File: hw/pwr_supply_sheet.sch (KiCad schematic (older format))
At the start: 12 parts

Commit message: porting uv0a_hds pcb to uw_display
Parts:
- removed C11: 10nF, kemet:Kemet-CAPC1608X85N, symbol 10nF
- removed C13, C9: 100nF, kemet:Kemet-CAPC1608X85N, symbol 100nF
- removed L201: IND_744045210, usevolt:IND_744045210, symbol IND_744045210
- removed VR1: LM2671SOIC8, usevolt:SOIC8, symbol LM2671SOIC8-RESCUE-display
- added C203, C204, C205: 100nF, kemet:0603, symbol 100nF
- added L201: INDUCTOR_SDR1005-101KL, usevolt:INDUCTOR_BOURNS_10X13X5MM, symbol INDUCTOR_SDR1005-101KL
- added VR201: LM2671SOIC8, usevolt:SOIC8, symbol LM2671SOIC8
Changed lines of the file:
@@
 $Descr A4 11693 8268
 encoding utf-8
-Sheet 2 3
+Sheet 2 5
 Title "Power supply"
 Date "2016-08-20"
@@
 	1    3000 4050
 	0    -1   -1   0
-$EndComp
-$Comp
-L 100nF C9
-U 1 1 57B8217A
-P 3200 3950
-F 0 "C9" V 3208 4023 45  0000 L CNN
-F 1 "100nF" V 3292 4023 45  0000 L CNN
-F 2 "kemet:Kemet-CAPC1608X85N" H 3230 4100 20  0001 C CNN
-F 3 "http://www.farnell.com/datasheets/2062872.pdf?_ga=1.250530118.1948984246.1460023966" H 3104 3959 60  0001 C CNN
-F 4 "1288255" H 3504 4359 60  0001 C CNN "1st Source Part Number"
-F 5 "C0603C104K5RACTU" H 3304 4159 60  0001 C CNN "Manufacturer Part Number"
-F 6 "Farnell" H 3404 4259 60  0001 C CNN "1st Source"
-F 7 "KEMET" H 3204 4059 60  0001 C CNN "Manufacturer"
-	1    3200 3950
-	0    1    1    0
-$EndComp
-$Comp
-L LM2671SOIC8-RESCUE-display VR1
-U 1 1 57B82261
-P 4850 4150
-AR Path="/57B82261" Ref="VR1"  Part="1"
-AR Path="/57B81D4F/57B82261" Ref="VR1"  Part="1"
-F 0 "VR1" H 5050 4804 45  0000 C CNN
-F 1 "LM2671SOIC8" H 5050 4720 45  0000 C CNN
-F 2 "usevolt:SOIC8" H 4880 4300 20  0001 C CNN
-F 3 "http://www.farnell.com/datasheets/1902681.pdf?_ga=1.246738500.1948984246.1460023966" H 4650 4670 60  0001 C CNN
-F 4 "1469200" H 5050 5070 60  0001 C CNN "1st Source Part Number"
-F 5 "926-LM2671M-5.0/NOPB" H 5250 5270 60  0001 C CNN "2nd Source Part Number"
-F 6 "Farnell" H 4950 4970 60  0001 C CNN "1st Source"
-F 7 "LM2671M-5.0/NOPB" H 4850 4870 60  0001 C CNN "Manufacturer Part Number"
-F 8 "Mouser" H 5150 5170 60  0001 C CNN "2nd Source"
-F 9 "TEXAS INSTRUMENTS" H 4750 4770 60  0001 C CNN "Manufacturer"
-	1    4850 4150
-	1    0    0    -1
-$EndComp
-$Comp
-L 10nF C11
-U 1 1 57B822C5
-P 5800 3950
-F 0 "C11" H 5850 4149 45  0000 C CNN
-F 1 "10nF" H 5850 4065 45  0000 C CNN
-F 2 "kemet:Kemet-CAPC1608X85N" H 5830 4100 20  0001 C CNN
-F 3 "http://www.farnell.com/datasheets/2064086.pdf?_ga=1.250530118.1948984246.1460023966" H 5704 3959 60  0001 C CNN
-F 4 "1457729" H 6104 4359 60  0001 C CNN "1st Source Part Number"
-F 5 "C0603C103J3GACTU" H 5904 4159 60  0001 C CNN "Manufacturer Part Number"
-F 6 "Farnell" H 6004 4259 60  0001 C CNN "1st Source"
-F 7 "KEMET" H 5804 4059 60  0001 C CNN "Manufacturer"
-	1    5800 3950
-	1    0    0    -1
 $EndComp
 $Comp
@@
 	1    0    0    -1
 $EndComp
-$Comp
-L 100nF C13
-U 1 1 57B82A3F
-P 8600 3950
-F 0 "C13" V 8608 4023 45  0000 L CNN
-F 1 "100nF" V 8692 4023 45  0000 L CNN
-F 2 "kemet:Kemet-CAPC1608X85N" H 8630 4100 20  0001 C CNN
-F 3 "http://www.farnell.com/datasheets/2062872.pdf?_ga=1.250530118.1948984246.1460023966" H 8504 3959 60  0001 C CNN
-F 4 "1288255" H 8904 4359 60  0001 C CNN "1st Source Part Number"
-F 5 "C0603C104K5RACTU" H 8704 4159 60  0001 C CNN "Manufacturer Part Number"
-F 6 "Farnell" H 8804 4259 60  0001 C CNN "1st Source"
-F 7 "KEMET" H 8604 4059 60  0001 C CNN "Manufacturer"
-	1    8600 3950
-	0    1    1    0
-$EndComp
 Wire Wire Line
 	8000 4300 8000 4250
@@
 VLCD
 $Comp
-L IND_744045210 L201
-U 1 1 594FF8F5
+L INDUCTOR_SDR1005-101KL L201
+U 1 1 5A0C53F2
 P 6500 3850
 F 0 "L201" H 6500 4041 45  0000 C CNN
-F 1 "IND_744045210" H 6500 3957 45  0000 C CNN
-F 2 "usevolt:IND_744045210" H 6530 4000 20  0001 C CNN
-F 3 "http://www.farnell.com/datasheets/1735442.pdf?_ga=1.223184091.1948984246.1460023966" H 6400 3790 60  0001 C CNN
-F 4 "1800416" H 6800 4190 60  0001 C CNN "1st Source Part Number"
-F 5 "WURTH ELEKTRONIK" H 6500 3890 60  0001 C CNN "Manufacturer"
+F 1 "INDUCTOR_SDR1005-101KL" H 6500 3957 45  0000 C CNN
+F 2 "usevolt:INDUCTOR_BOURNS_10X13X5MM" H 6530 4000 20  0001 C CNN
+F 3 "http://www.farnell.com/datasheets/1695384.pdf?_ga=1.223340891.1948984246.1460023966" H 6400 3790 60  0001 C CNN
+F 4 "1828057" H 6800 4190 60  0001 C CNN "1st Source Part Number"
+F 5 "BOURNS" H 6500 3890 60  0001 C CNN "Manufacturer"
 F 6 "Digi-Key" H 6900 4290 60  0001 C CNN "2nd Source"
 F 7 "Farnell" H 6700 4090 60  0001 C CNN "1st Source"
-F 8 "744045210" H 6600 3990 60  0001 C CNN "Manufacturer Part Number"
-F 9 "732-3072-1-ND" H 7000 4390 60  0001 C CNN "2nd Source Part Number"
+F 8 "SDR1005-101KL" H 6600 3990 60  0001 C CNN "Manufacturer Part Number"
+F 9 "SDR1005-101KLCT-ND" H 7000 4390 60  0001 C CNN "2nd Source Part Number"
 	1    6500 3850
 	1    0    0    -1
 $EndComp
+$Comp
+L LM2671SOIC8 VR201
+U 1 1 5A0C5926
+P 4850 4150
+F 0 "VR201" H 5050 4804 45  0000 C CNN
+F 1 "LM2671SOIC8" H 5050 4720 45  0000 C CNN
+F 2 "usevolt:SOIC8" H 4880 4300 20  0001 C CNN
+F 3 "http://www.farnell.com/datasheets/1902681.pdf?_ga=1.246738500.1948984246.1460023966" H 4650 4670 60  0001 C CNN
+F 4 "1469200" H 5050 5070 60  0001 C CNN "1st Source Part Number"
+F 5 "926-LM2671M-5.0/NOPB" H 5250 5270 60  0001 C CNN "2nd Source Part Number"
+F 6 "Farnell" H 4950 4970 60  0001 C CNN "1st Source"
+F 7 "LM2671M-5.0/NOPB" H 4850 4870 60  0001 C CNN "Manufacturer Part Number"
+F 8 "Mouser" H 5150 5170 60  0001 C CNN "2nd Source"
+F 9 "TEXAS INSTRUMENTS" H 4750 4770 60  0001 C CNN "Manufacturer"
+	1    4850 4150
+	1    0    0    -1
+$EndComp
+$Comp
+L 100nF C204
+U 1 1 5A0C68D3
+P 5800 3950
+F 0 "C204" H 5850 4149 45  0000 C CNN
+F 1 "100nF" H 5850 4065 45  0000 C CNN
+F 2 "kemet:0603" H 5830 4100 20  0001 C CNN
+F 3 "http://www.farnell.com/datasheets/2062872.pdf?_ga=1.250530118.1948984246.1460023966" H 5704 3959 60  0001 C CNN
+F 4 "1288255" H 6104 4359 60  0001 C CNN "1st Source Part Number"
+F 5 "C0603C104K5RACTU" H 5904 4159 60  0001 C CNN "Manufacturer Part Number"
+F 6 "Farnell" H 6004 4259 60  0001 C CNN "1st Source"
+F 7 "KEMET" H 5804 4059 60  0001 C CNN "Manufacturer"
+	1    5800 3950
+	1    0    0    -1
+$EndComp
+$Comp
+L 100nF C205
+U 1 1 5A0C6963
+P 8600 3950
+F 0 "C205" V 8608 4023 45  0000 L CNN
+F 1 "100nF" V 8692 4023 45  0000 L CNN
+F 2 "kemet:0603" H 8630 4100 20  0001 C CNN
+F 3 "http://www.farnell.com/datasheets/2062872.pdf?_ga=1.250530118.1948984246.1460023966" H 8504 3959 60  0001 C CNN
+F 4 "1288255" H 8904 4359 60  0001 C CNN "1st Source Part Number"
+F 5 "C0603C104K5RACTU" H 8704 4159 60  0001 C CNN "Manufacturer Part Number"
+F 6 "Farnell" H 8804 4259 60  0001 C CNN "1st Source"
+F 7 "KEMET" H 8604 4059 60  0001 C CNN "Manufacturer"
+	1    8600 3950
+	0    1    1    0
+$EndComp
+$Comp
+L 100nF C203
+U 1 1 5A0C6A34
+P 3200 3950
+F 0 "C203" V 3208 4023 45  0000 L CNN
+F 1 "100nF" V 3292 4023 45  0000 L CNN
+F 2 "kemet:0603" H 3230 4100 20  0001 C CNN
+F 3 "http://www.farnell.com/datasheets/2062872.pdf?_ga=1.250530118.1948984246.1460023966" H 3104 3959 60  0001 C CNN
+F 4 "1288255" H 3504 4359 60  0001 C CNN "1st Source Part Number"
+F 5 "C0603C104K5RACTU" H 3304 4159 60  0001 C CNN "Manufacturer Part Number"
+F 6 "Farnell" H 3404 4259 60  0001 C CNN "1st Source"
+F 7 "KEMET" H 3204 4059 60  0001 C CNN "Manufacturer"
+	1    3200 3950
+	0    1    1    0
+$EndComp
 $EndSCHEMATC

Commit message: 1.7.0 pcb created, not yet ordered
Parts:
- removed C201: T491D226K035AT, kemet:7343, symbol T491D226K035AT
- added C201: CAP_EEE-FK1H470P, usevolt:CAP_EEE-FK1H470P, symbol CAP_EEE-FK1H470P
- added F202: FUSE_MC36211_350MA, usevolt:FUSE_MC36211, symbol FUSE_MC36211_350MA
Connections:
- net GND: now also C201.-
- net VDD: now also C201.+
- net VIN: now also F202.P$1
- net VLCD: now also F202.P$2
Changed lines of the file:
@@
 	3400 3550 3400 3850
 $Comp
-L VDD #PWR201
+L VDD #PWR08
 U 1 1 57B83157
 P 3400 3550
-F 0 "#PWR201" H 3400 3400 50  0001 C CNN
+F 0 "#PWR08" H 3400 3400 50  0001 C CNN
 F 1 "VDD" H 3417 3723 50  0000 C CNN
 F 2 "" H 3400 3550 50  0000 C CNN
@@
 	1    0    0    -1
 $EndComp
-Connection ~ 3400 3750
-$Comp
-L +5V #PWR204
+$Comp
+L +5V #PWR09
 U 1 1 57B831F8
 P 6850 3600
-F 0 "#PWR204" H 6850 3450 50  0001 C CNN
+F 0 "#PWR09" H 6850 3450 50  0001 C CNN
 F 1 "+5V" H 6865 3773 50  0000 C CNN
 F 2 "" H 6850 3600 50  0000 C CNN
@@
 Connection ~ 6850 3750
 $Comp
-L +3V3 #PWR205
+L +3V3 #PWR010
 U 1 1 57B83259
 P 8600 3600
-F 0 "#PWR205" H 8600 3450 50  0001 C CNN
+F 0 "#PWR010" H 8600 3450 50  0001 C CNN
 F 1 "+3V3" H 8615 3773 50  0000 C CNN
 F 2 "" H 8600 3600 50  0000 C CNN
@@
 NoConn ~ 4550 4050
 $Comp
-L VDD #PWR202
+L VDD #PWR011
 U 1 1 57B9C56A
 P 3800 2100
-F 0 "#PWR202" H 3800 1950 50  0001 C CNN
+F 0 "#PWR011" H 3800 1950 50  0001 C CNN
 F 1 "VDD" H 3817 2273 50  0000 C CNN
 F 2 "" H 3800 2100 50  0000 C CNN
@@
 $EndComp
 $Comp
-L PWR_FLAG #FLG201
+L PWR_FLAG #FLG012
 U 1 1 57B9C59C
 P 3800 2300
-F 0 "#FLG201" H 3800 2395 50  0001 C CNN
+F 0 "#FLG012" H 3800 2395 50  0001 C CNN
 F 1 "PWR_FLAG" H 3800 2523 50  0000 C CNN
 F 2 "" H 3800 2300 50  0000 C CNN
@@
 	3800 2300 3800 2100
 $Comp
-L GND #PWR203
+L GND #PWR013
 U 1 1 57B9D351
 P 4300 2350
-F 0 "#PWR203" H 4300 2100 50  0001 C CNN
+F 0 "#PWR013" H 4300 2100 50  0001 C CNN
 F 1 "GND" H 4305 2177 50  0000 C CNN
 F 2 "" H 4300 2350 50  0000 C CNN
@@
 $EndComp
 $Comp
-L PWR_FLAG #FLG202
+L PWR_FLAG #FLG014
 U 1 1 57B9D3A1
 P 4300 2150
-F 0 "#FLG202" H 4300 2245 50  0001 C CNN
+F 0 "#FLG014" H 4300 2245 50  0001 C CNN
 F 1 "PWR_FLAG" H 4300 2374 50  0000 C CNN
 F 2 "" H 4300 2150 50  0000 C CNN
@@
 $EndComp
 $Comp
-L T491D226K035AT C201
-U 1 1 58F3D42E
-P 3400 4050
-F 0 "C201" V 3308 4153 45  0000 L CNN
-F 1 "T491D226K035AT" V 3392 4153 45  0000 L CNN
-F 2 "kemet:7343" H 3430 4200 20  0001 C CNN
-F 3 "http://www.farnell.com/datasheets/2121523.pdf?_ga=1.259966538.1948984246.1460023966" H 3400 3990 60  0001 C CNN
-F 4 "399-8375-1-ND" H 4000 4590 60  0001 C CNN "2nd Source Part Number"
-F 5 "Farnell" H 3700 4290 60  0001 C CNN "1st Source"
-F 6 "T491D226K035AT" H 3600 4190 60  0001 C CNN "Manufacturer Part Number"
-F 7 "Digikey" H 3900 4490 60  0001 C CNN "2nd Source"
-F 8 "Kemet" H 3500 4090 60  0001 C CNN "Manufacturer"
-F 9 "1457504" H 3800 4390 60  0001 C CNN "1st Source Part Number"
-	1    3400 4050
-	0    1    1    0
-$EndComp
-$Comp
 L FUSE_MC36211_350MA F201
 U 1 1 594FEE3D
@@
 $EndComp
 Wire Wire Line
-	2150 3850 2150 3050
+	2150 2700 2150 3850
 Wire Wire Line
 	2150 3050 2500 3050
@@
 	0    1    1    0
 $EndComp
+$Comp
+L FUSE_MC36211_350MA F202
+U 1 1 5A0D6608
+P 2700 2700
+F 0 "F202" H 2700 2904 45  0000 C CNN
+F 1 "FUSE_MC36211_350MA" H 2700 2820 45  0000 C CNN
+F 2 "usevolt:FUSE_MC36211" H 2730 2850 20  0001 C CNN
+F 3 "http://www.farnell.com/datasheets/1678471.pdf?_ga=1.218604761.1948984246.1460023966" H 2820 2720 60  0001 C CNN
+F 4 "Farnell" H 3120 3020 60  0001 C CNN "1st Source"
+F 5 "MC36211" H 3020 2920 60  0001 C CNN "Manufacturer Part Number"
+F 6 "MC36211" H 3220 3120 60  0001 C CNN "1st Source Part Number"
+F 7 "Multicomp" H 2920 2820 60  0001 C CNN "Manufacturer"
+	1    2700 2700
+	1    0    0    -1
+$EndComp
+Wire Wire Line
+	2500 2700 2150 2700
+Connection ~ 2150 3050
+Wire Wire Line
+	2900 2700 3200 2700
+Wire Wire Line
+	3200 2700 3200 3050
+Connection ~ 3200 3050
+$Comp
+L CAP_EEE-FK1H470P C201
+U 1 1 5A1029C5
+P 3400 4050
+F 0 "C201" V 3308 4153 45  0000 L CNN
+F 1 "CAP_EEE-FK1H470P" V 3392 4153 45  0000 L CNN
+F 2 "usevolt:CAP_EEE-FK1H470P" H 3430 4200 20  0001 C CNN
+F 3 "http://industrial.panasonic.com/www-cgi/jvcr13pz.cgi?E+PZ+3+ABA0120+EEEFK1H470P+7+WW" H 3400 3990 60  0001 C CNN
+F 4 "667-EEE-FK1H470P" H 4000 4590 60  0001 C CNN "2nd Source Part Number"
+F 5 "Digi-Key" H 3700 4290 60  0001 C CNN "1st Source"
+F 6 "EEE-FK1H470P" H 3600 4190 60  0001 C CNN "Manufacturer Part Number"
+F 7 "Mouser" H 3900 4490 60  0001 C CNN "2nd Source"
+F 8 "Panasonic Electronic Components" H 3500 4090 60  0001 C CNN "Manufacturer"
+F 9 "PCE3815CT-ND" H 3800 4390 60  0001 C CNN "1st Source Part Number"
+	1    3400 4050
+	0    1    1    0
+$EndComp
+Connection ~ 3400 3850
 $EndSCHEMATC

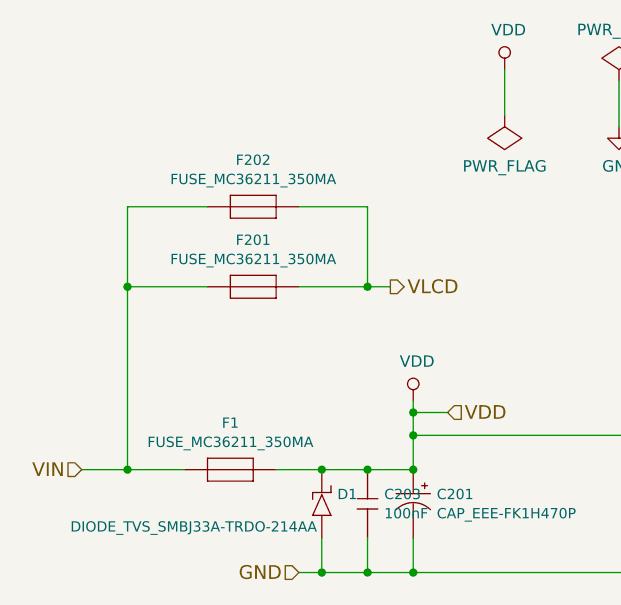
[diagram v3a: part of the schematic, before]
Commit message: hw 2.1.0 with LPC1549 & FT812 ordered from seeed
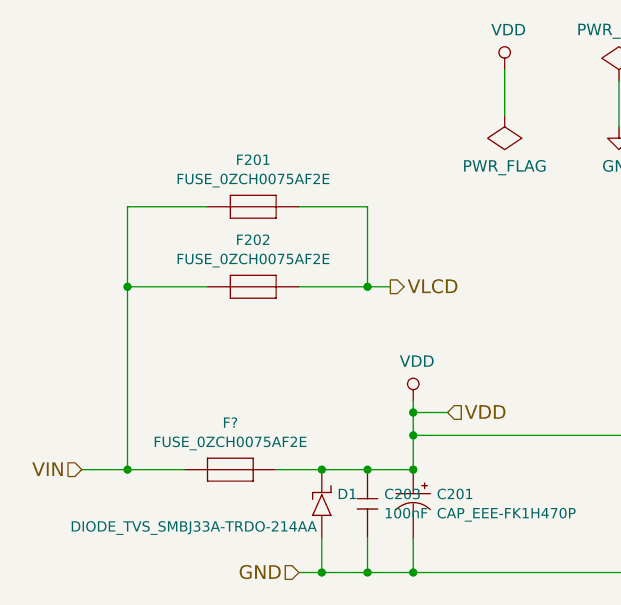
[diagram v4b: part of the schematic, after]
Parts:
- removed F1, F201, F202: FUSE_MC36211_350MA, usevolt:FUSE_MC36211, symbol FUSE_MC36211_350MA
- added F201, F202, F?: FUSE_0ZCH0075AF2E, usevolt:1210, symbol FUSE_0ZCH0075AF2E
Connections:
- net VDD: now also F?.2
- net VIN: now also F201.1, F202.1, F?.1
- net VLCD: now also F201.2, F202.2
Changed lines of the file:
@@
 VIN
-$Comp
-L FUSE_MC36211_350MA F1
-U 1 1 57B8204F
-P 2600 3850
-F 0 "F1" H 2600 4054 45  0000 C CNN
-F 1 "FUSE_MC36211_350MA" H 2600 3970 45  0000 C CNN
-F 2 "usevolt:FUSE_MC36211" H 2630 4000 20  0001 C CNN
-F 3 "http://www.farnell.com/datasheets/1678471.pdf?_ga=1.218604761.1948984246.1460023966" H 2720 3870 60  0001 C CNN
-F 4 "Farnell" H 3020 4170 60  0001 C CNN "1st Source"
-F 5 "MC36211" H 2920 4070 60  0001 C CNN "Manufacturer Part Number"
-F 6 "MC36211" H 3120 4270 60  0001 C CNN "1st Source Part Number"
-F 7 "Multicomp" H 2820 3970 60  0001 C CNN "Manufacturer"
-	1    2600 3850
-	1    0    0    -1
-$EndComp
 $Comp
 L DIODE_TVS_SMBJ33A-TRDO-214AA D1
@@
 $EndComp
 Wire Wire Line
-	2400 3850 1950 3850
+	1950 3850 2400 3850
 Wire Wire Line
 	3400 3700 4550 3700
@@
 	0    1    1    0
 $EndComp
-$Comp
-L FUSE_MC36211_350MA F201
-U 1 1 594FEE3D
-P 2700 3050
-F 0 "F201" H 2700 3254 45  0000 C CNN
-F 1 "FUSE_MC36211_350MA" H 2700 3170 45  0000 C CNN
-F 2 "usevolt:FUSE_MC36211" H 2730 3200 20  0001 C CNN
-F 3 "http://www.farnell.com/datasheets/1678471.pdf?_ga=1.218604761.1948984246.1460023966" H 2820 3070 60  0001 C CNN
-F 4 "Farnell" H 3120 3370 60  0001 C CNN "1st Source"
-F 5 "MC36211" H 3020 3270 60  0001 C CNN "Manufacturer Part Number"
-F 6 "MC36211" H 3220 3470 60  0001 C CNN "1st Source Part Number"
-F 7 "Multicomp" H 2920 3170 60  0001 C CNN "Manufacturer"
-	1    2700 3050
-	1    0    0    -1
-$EndComp
 Wire Wire Line
 	2150 2700 2150 3850
@@
 	1    3200 3950
 	0    1    1    0
-$EndComp
-$Comp
-L FUSE_MC36211_350MA F202
-U 1 1 5A0D6608
-P 2700 2700
-F 0 "F202" H 2700 2904 45  0000 C CNN
-F 1 "FUSE_MC36211_350MA" H 2700 2820 45  0000 C CNN
-F 2 "usevolt:FUSE_MC36211" H 2730 2850 20  0001 C CNN
-F 3 "http://www.farnell.com/datasheets/1678471.pdf?_ga=1.218604761.1948984246.1460023966" H 2820 2720 60  0001 C CNN
-F 4 "Farnell" H 3120 3020 60  0001 C CNN "1st Source"
-F 5 "MC36211" H 3020 2920 60  0001 C CNN "Manufacturer Part Number"
-F 6 "MC36211" H 3220 3120 60  0001 C CNN "1st Source Part Number"
-F 7 "Multicomp" H 2920 2820 60  0001 C CNN "Manufacturer"
-	1    2700 2700
-	1    0    0    -1
 $EndComp
 Wire Wire Line
@@
 $EndComp
 Connection ~ 3400 3850
+$Comp
+L FUSE_0ZCH0075AF2E F202
+U 1 1 5A399EB3
+P 2700 3050
+F 0 "F202" H 2700 3254 45  0000 C CNN
+F 1 "FUSE_0ZCH0075AF2E" H 2700 3170 45  0000 C CNN
+F 2 "usevolt:1210" H 2730 3200 20  0001 C CNN
+F 3 "https://belfuse.com/resources/CircuitProtection/datasheets/0ZCH%20Nov2016.pdf" H 2820 3070 60  0001 C CNN
+F 4 "507-1788-1-ND" H 3220 3470 60  0001 C CNN "1st Source Part Number"
+F 5 "Digikey" H 3120 3370 60  0001 C CNN "1st Source"
+F 6 "0ZCH0075AF2E" H 3020 3270 60  0001 C CNN "Manufacturer Part Number"
+F 7 "Bel Fuse Inc." H 2920 3170 60  0001 C CNN "Manufacturer"
+	1    2700 3050
+	1    0    0    -1
+$EndComp
+$Comp
+L FUSE_0ZCH0075AF2E F201
+U 1 1 5A399F0F
+P 2700 2700
+F 0 "F201" H 2700 2904 45  0000 C CNN
+F 1 "FUSE_0ZCH0075AF2E" H 2700 2820 45  0000 C CNN
+F 2 "usevolt:1210" H 2730 2850 20  0001 C CNN
+F 3 "https://belfuse.com/resources/CircuitProtection/datasheets/0ZCH%20Nov2016.pdf" H 2820 2720 60  0001 C CNN
+F 4 "507-1788-1-ND" H 3220 3120 60  0001 C CNN "1st Source Part Number"
+F 5 "Digikey" H 3120 3020 60  0001 C CNN "1st Source"
+F 6 "0ZCH0075AF2E" H 3020 2920 60  0001 C CNN "Manufacturer Part Number"
+F 7 "Bel Fuse Inc." H 2920 2820 60  0001 C CNN "Manufacturer"
+	1    2700 2700
+	1    0    0    -1
+$EndComp
+$Comp
+L FUSE_0ZCH0075AF2E F?
+U 1 1 5A39B376
+P 2600 3850
+F 0 "F?" H 2600 4054 45  0000 C CNN
+F 1 "FUSE_0ZCH0075AF2E" H 2600 3970 45  0000 C CNN
+F 2 "usevolt:1210" H 2630 4000 20  0001 C CNN
+F 3 "https://belfuse.com/resources/CircuitProtection/datasheets/0ZCH%20Nov2016.pdf" H 2720 3870 60  0001 C CNN
+F 4 "507-1788-1-ND" H 3120 4270 60  0001 C CNN "1st Source Part Number"
+F 5 "Digikey" H 3020 4170 60  0001 C CNN "1st Source"
+F 6 "0ZCH0075AF2E" H 2920 4070 60  0001 C CNN "Manufacturer Part Number"
+F 7 "Bel Fuse Inc." H 2820 3970 60  0001 C CNN "Manufacturer"
+	1    2600 3850
+	1    0    0    -1
+$EndComp
 $EndSCHEMATC

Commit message: 2.1.0 schematic updates committed
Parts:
- gave numbers to parts that had none: 1
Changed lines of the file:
@@
 	3400 3550 3400 3850
 $Comp
-L VDD #PWR08
+L VDD #PWR201
 U 1 1 57B83157
 P 3400 3550
-F 0 "#PWR08" H 3400 3400 50  0001 C CNN
+F 0 "#PWR201" H 3400 3400 50  0001 C CNN
 F 1 "VDD" H 3417 3723 50  0000 C CNN
 F 2 "" H 3400 3550 50  0000 C CNN
@@
 $EndComp
 $Comp
-L +5V #PWR09
+L +5V #PWR204
 U 1 1 57B831F8
 P 6850 3600
-F 0 "#PWR09" H 6850 3450 50  0001 C CNN
+F 0 "#PWR204" H 6850 3450 50  0001 C CNN
 F 1 "+5V" H 6865 3773 50  0000 C CNN
 F 2 "" H 6850 3600 50  0000 C CNN
@@
 Connection ~ 6850 3750
 $Comp
-L +3V3 #PWR010
+L +3V3 #PWR205
 U 1 1 57B83259
 P 8600 3600
-F 0 "#PWR010" H 8600 3450 50  0001 C CNN
+F 0 "#PWR205" H 8600 3450 50  0001 C CNN
 F 1 "+3V3" H 8615 3773 50  0000 C CNN
 F 2 "" H 8600 3600 50  0000 C CNN
@@
 NoConn ~ 4550 4050
 $Comp
-L VDD #PWR011
+L VDD #PWR202
 U 1 1 57B9C56A
 P 3800 2100
-F 0 "#PWR011" H 3800 1950 50  0001 C CNN
+F 0 "#PWR202" H 3800 1950 50  0001 C CNN
 F 1 "VDD" H 3817 2273 50  0000 C CNN
 F 2 "" H 3800 2100 50  0000 C CNN
@@
 $EndComp
 $Comp
-L PWR_FLAG #FLG012
+L PWR_FLAG #FLG201
 U 1 1 57B9C59C
 P 3800 2300
-F 0 "#FLG012" H 3800 2395 50  0001 C CNN
+F 0 "#FLG201" H 3800 2395 50  0001 C CNN
 F 1 "PWR_FLAG" H 3800 2523 50  0000 C CNN
 F 2 "" H 3800 2300 50  0000 C CNN
@@
 	3800 2300 3800 2100
 $Comp
-L GND #PWR013
+L GND #PWR203
 U 1 1 57B9D351
 P 4300 2350
-F 0 "#PWR013" H 4300 2100 50  0001 C CNN
+F 0 "#PWR203" H 4300 2100 50  0001 C CNN
 F 1 "GND" H 4305 2177 50  0000 C CNN
 F 2 "" H 4300 2350 50  0000 C CNN
@@
 $EndComp
 $Comp
-L PWR_FLAG #FLG014
+L PWR_FLAG #FLG202
 U 1 1 57B9D3A1
 P 4300 2150
-F 0 "#FLG014" H 4300 2245 50  0001 C CNN
+F 0 "#FLG202" H 4300 2245 50  0001 C CNN
 F 1 "PWR_FLAG" H 4300 2374 50  0000 C CNN
 F 2 "" H 4300 2150 50  0000 C CNN
@@
 $EndComp
 $Comp
-L FUSE_0ZCH0075AF2E F?
+L FUSE_0ZCH0075AF2E F203
 U 1 1 5A39B376
 P 2600 3850
-F 0 "F?" H 2600 4054 45  0000 C CNN
+F 0 "F203" H 2600 4054 45  0000 C CNN
 F 1 "FUSE_0ZCH0075AF2E" H 2600 3970 45  0000 C CNN
 F 2 "usevolt:1210" H 2630 4000 20  0001 C CNN
